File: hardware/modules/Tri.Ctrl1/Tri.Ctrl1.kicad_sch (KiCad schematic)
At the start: 1 part

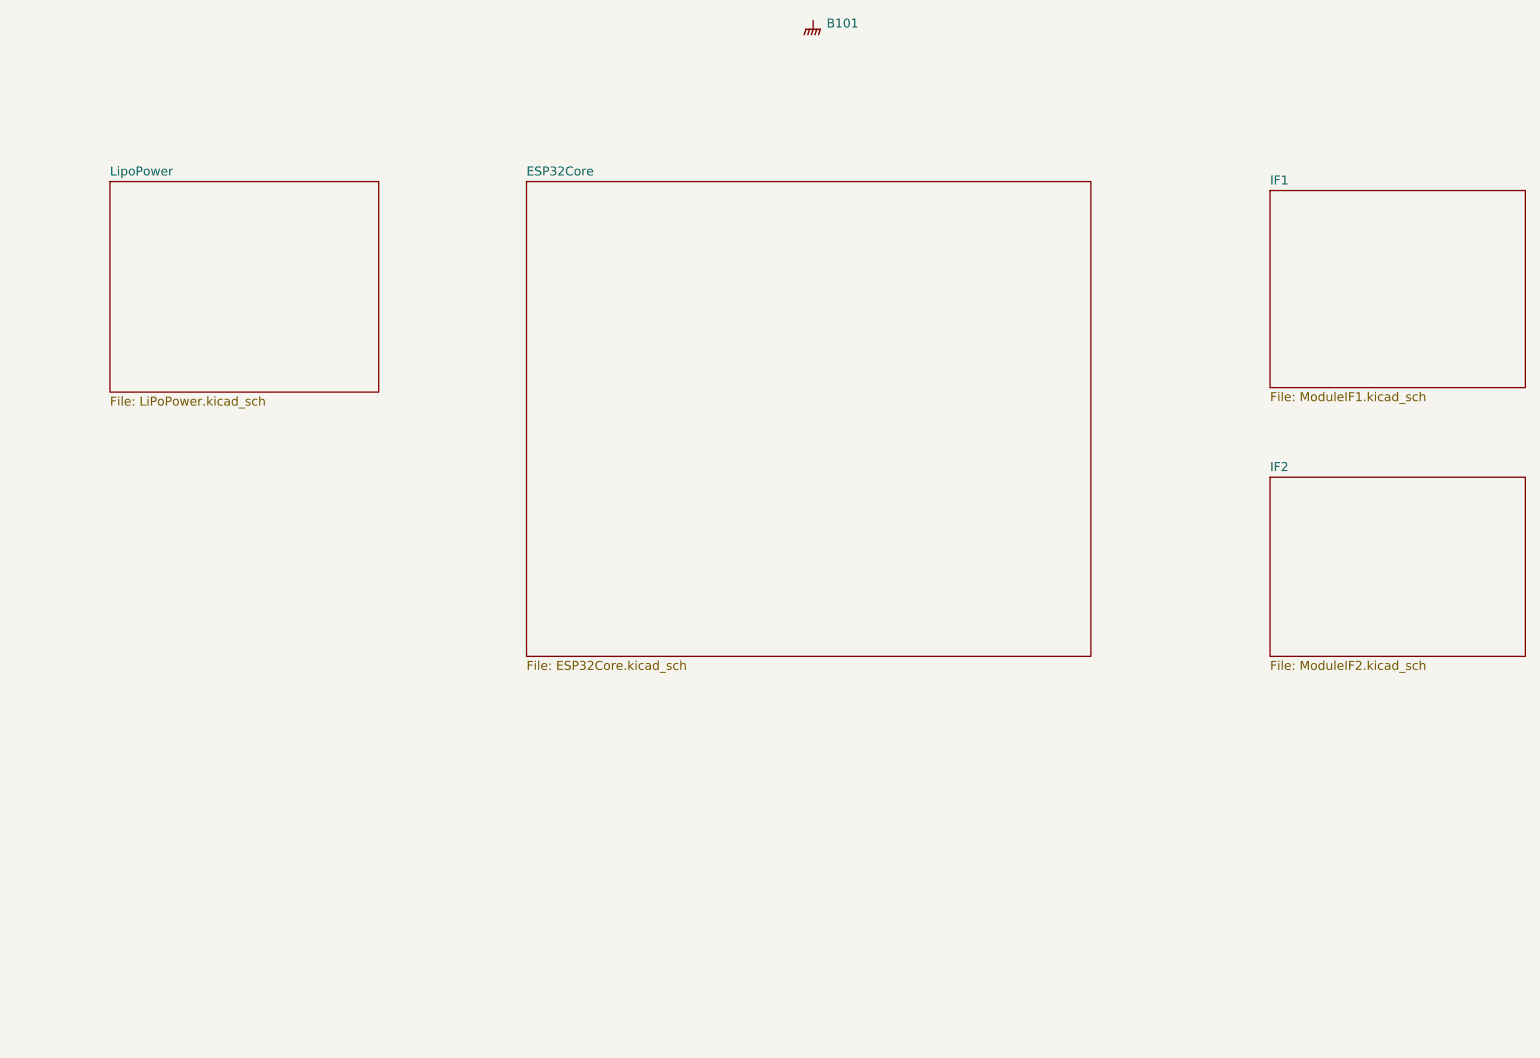
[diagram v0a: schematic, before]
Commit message: 回路図　半分終わり
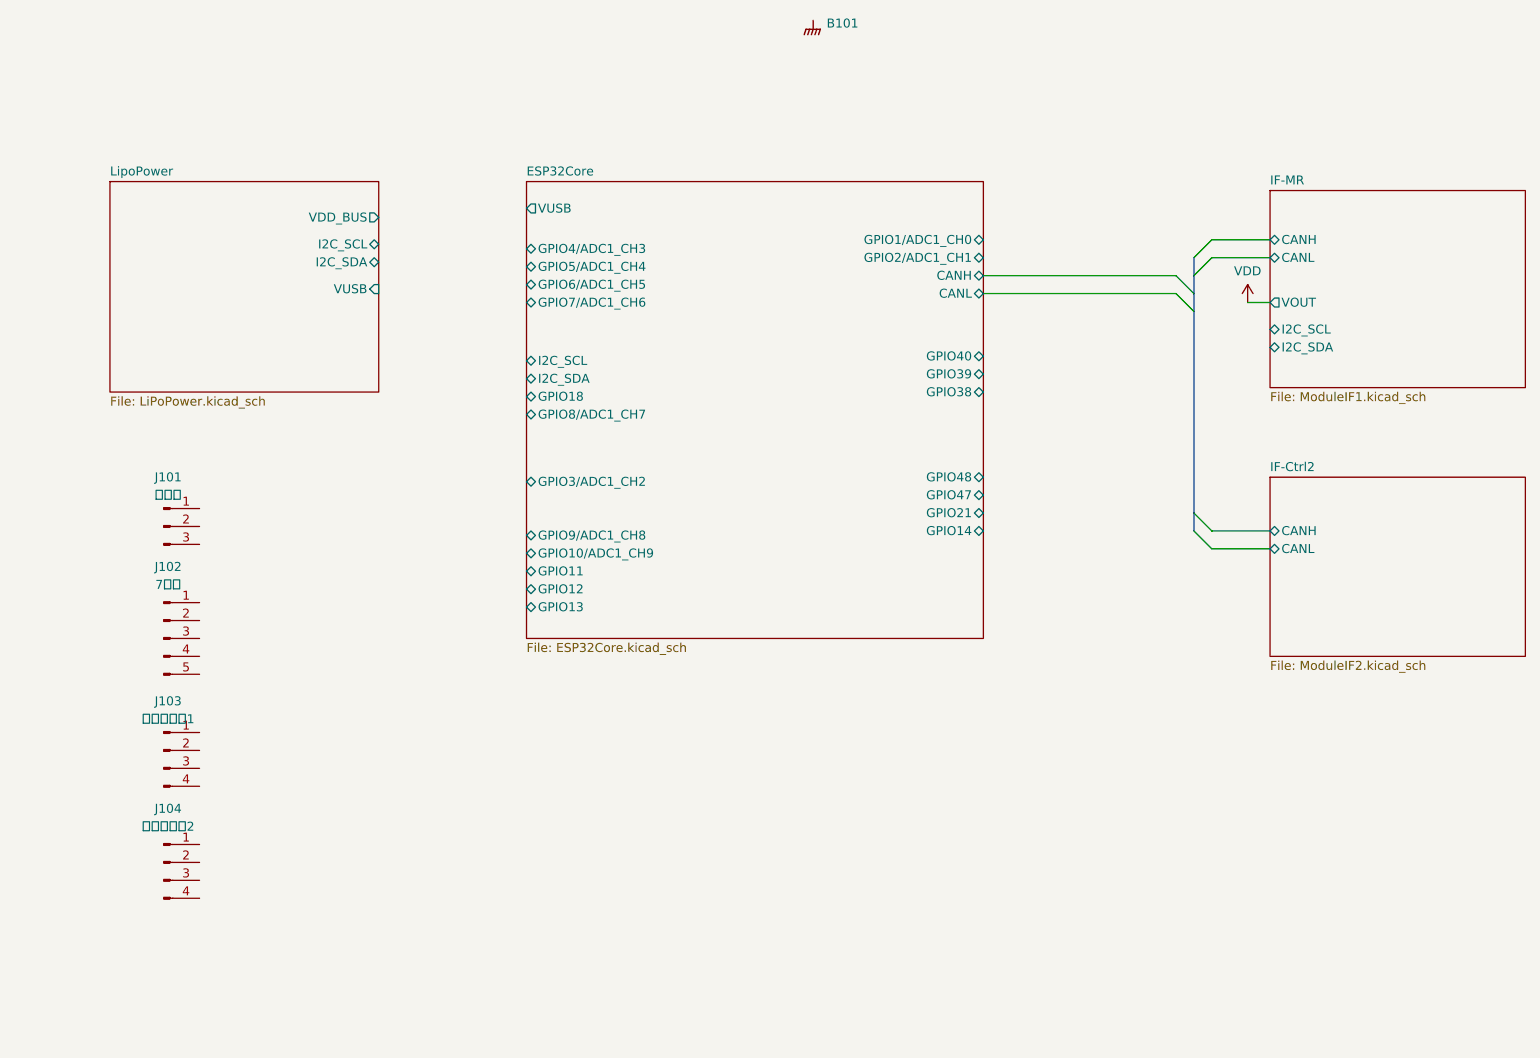
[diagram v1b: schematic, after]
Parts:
- added J101: トリム, symbol Connector:Conn_01x03_Pin
- added J102: 7セグ, symbol Connector:Conn_01x05_Pin
- added J103: ジョイコン1, symbol Connector:Conn_01x04_Pin
- added J104: ジョイコン2, symbol Connector:Conn_01x04_Pin
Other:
- sheet IF1 renamed IF-MR
- sheet IF2 renamed IF-Ctrl2
- sheet ESP32Core ports: added CANH, CANL, GPIO10/ADC1_CH9, GPIO11, GPIO12, GPIO13, GPIO14, GPIO18, GPIO1/ADC1_CH0, GPIO21, GPIO2/ADC1_CH1, GPIO38, GPIO39, GPIO3/ADC1_CH2, GPIO40, GPIO47, GPIO48, GPIO4/ADC1_CH3, GPIO5/ADC1_CH4, GPIO6/ADC1_CH5, GPIO7/ADC1_CH6, GPIO8/ADC1_CH7, GPIO9/ADC1_CH8, I2C_SCL, I2C_SDA, VUSB; removed none
- sheet IF-Ctrl2 ports: added CANH, CANL; removed none
- sheet IF-MR ports: added CANH, CANL, I2C_SCL, I2C_SDA, VOUT; removed none
- sheet LipoPower ports: added I2C_SCL, I2C_SDA, VDD_BUS, VUSB; removed none

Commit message: 回路図終了
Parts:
- B101: footprint (none) -> WOBCLibrary:Board_1U_60x60
- J101: renamed from J103; footprint (none) -> Connector_JST:JST_XA_S04B-XASK-1N-BN_1x04_P2.50mm_Horizontal
- J102: renamed from J104; footprint (none) -> Connector_JST:JST_XA_S04B-XASK-1N-BN_1x04_P2.50mm_Horizontal
- J103: renamed from J101; footprint (none) -> Connector_JST:JST_XA_B03B-XASK-1_1x03_P2.50mm_Vertical
- J104: renamed from J102; footprint (none) -> Connector_JST:JST_XA_B05B-XASK-1_1x05_P2.50mm_Vertical
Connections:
- net ESP32Core/GPIO10/ADC1_CH9: now also J101.3 (Pin_3)
- net ESP32Core/GPIO11: now also J102.2 (Pin_2)
- net ESP32Core/GPIO12: now also J102.3 (Pin_3)
- net ESP32Core/GPIO9/ADC1_CH8: now also J101.2 (Pin_2)
- net GND: now also J101.4 (Pin_4), J102.4 (Pin_4), J103.3 (Pin_3), J104.2 (Pin_2)
- net VDD: now also J101.1 (Pin_1), J102.1 (Pin_1), J104.1 (Pin_1)
- net UP: now reaches J103.1 (Pin_1)
- net DOWN: now reaches J103.2 (Pin_2)
- net SDI: now reaches J104.3 (Pin_3)
- net SCK: now reaches J104.4 (Pin_4)
- net LATCH: now reaches J104.5 (Pin_5)
- no-connect marks 0 -> 12
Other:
- moved on the sheet: J101, J102, J103, J104

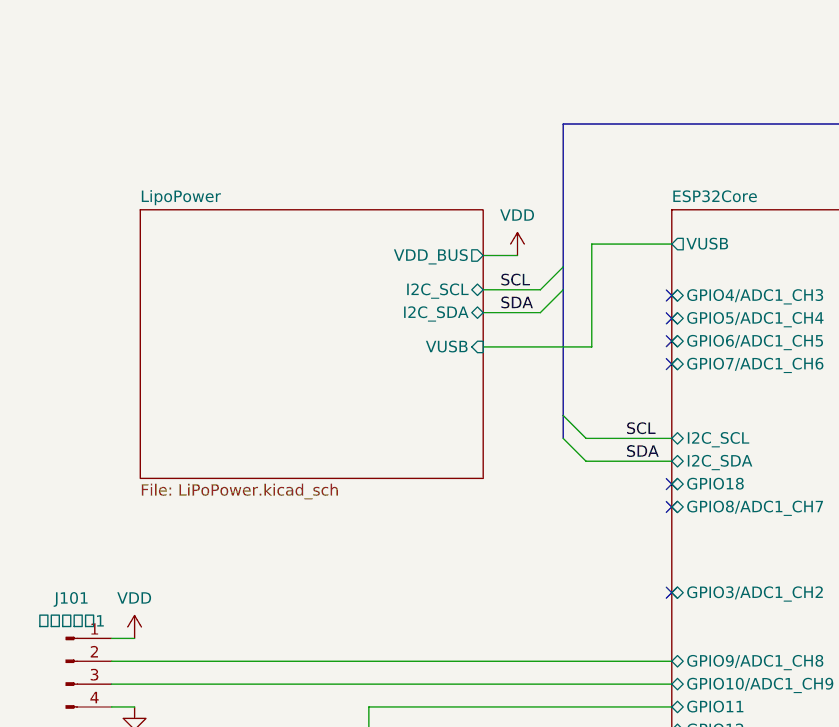
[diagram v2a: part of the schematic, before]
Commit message: 電源回路をlipoの充放電込みのモノに変更
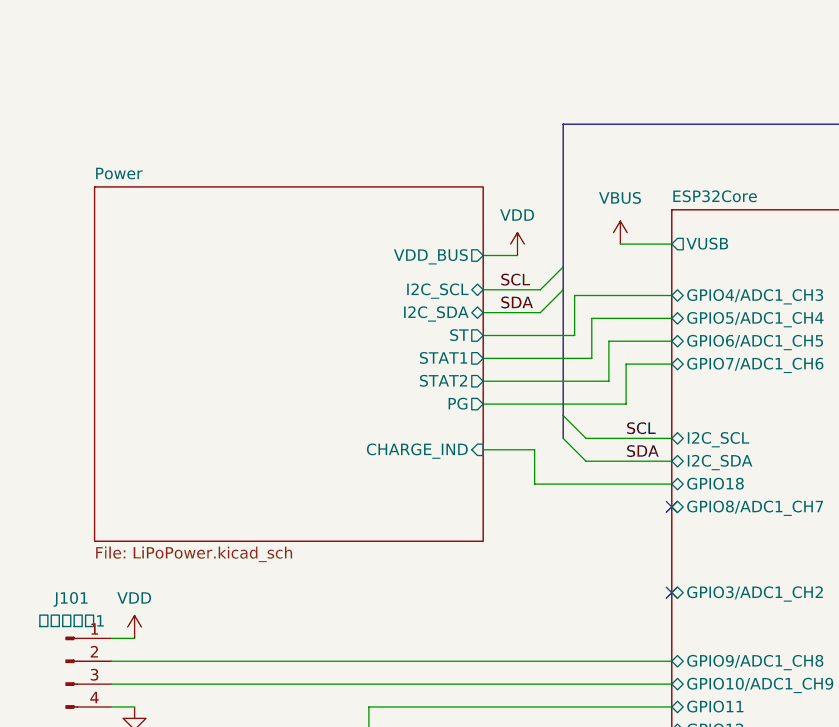
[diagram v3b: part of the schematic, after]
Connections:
- no-connect marks 12 -> 7
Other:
- removed sheet LipoPower
- added sheet Power (LiPoPower.kicad_sch)

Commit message: バックアップの回路削除
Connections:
- no-connect marks 7 -> 8
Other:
- sheet Power ports: added none; removed ST
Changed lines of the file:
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@@
 		(at 92.075 123.825)
+	)
+	(no_connect
+		(at 92.075 73.025)
 	)
 	(bus_entry
@@
 	(wire
 		(pts
-			(xy 92.075 73.025) (xy 81.28 73.025)
-		)
-		(stroke
-			(width 0)
-			(type default)
-		)
-	)
-	(wire
-		(pts
 			(xy 78.74 182.88) (xy 106.045 182.88)
 		)
@@
 	(wire
 		(pts
-			(xy 81.28 73.025) (xy 81.28 77.47)
-		)
-		(stroke
-			(width 0)
-			(type default)
-		)
-	)
-	(wire
-		(pts
 			(xy 156.845 76.835) (xy 184.15 76.835)
 		)
@@
 		(pts
 			(xy 71.12 80.01) (xy 83.185 80.01)
-		)
-		(stroke
-			(width 0)
-			(type default)
-		)
-	)
-	(wire
-		(pts
-			(xy 81.28 77.47) (xy 71.12 77.47)
 		)
 		(stroke
@@
 		(dnp no)
 		(fields_autoplaced yes)
-		(property "Reference" "#PWR0109"
+		(property "Reference" "#PWR0110"
 			(at 194.31 84.455 0)
 			(effects
@@
 			(project ""
 				(path "/39a3f286-a766-4612-a8bf-4e53d682d5ae"
-					(reference "#PWR0109")
+					(reference "#PWR0110")
 					(unit 1)
 				)
@@
 		(dnp no)
 		(fields_autoplaced yes)
-		(property "Reference" "#PWR0112"
+		(property "Reference" "#PWR0109"
 			(at 86.36 71.12 0)
 			(effects
@@
 			(project ""
 				(path "/39a3f286-a766-4612-a8bf-4e53d682d5ae"
-					(reference "#PWR0112")
+					(reference "#PWR0109")
 					(unit 1)
 				)
@@
 			(effects
 				(font
-					(size 1.27 1.27)
-				)
-				(justify right)
-			)
-		)
-		(pin "ST" output
-			(at 71.12 77.47 0)
-			(effects
-				(font

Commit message: 配置ちょっと進捗を
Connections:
- no-connect marks 8 -> 7
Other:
- sheet IF-MR ports: added EN, VIN; removed VOUT
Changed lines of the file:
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@@
-	)
-	(no_connect
-		(at 156.845 74.295)
 	)
 	(no_connect
@@
 	(wire
 		(pts
+			(xy 178.435 74.295) (xy 178.435 67.945)
+		)
+		(stroke
+			(width 0)
+			(type default)
+		)
+	)
+	(wire
+		(pts
 			(xy 189.23 113.03) (xy 197.485 113.03)
 		)
@@
 	(wire
 		(pts
+			(xy 178.435 67.945) (xy 197.485 67.945)
+		)
+		(stroke
+			(width 0)
+			(type default)
+		)
+	)
+	(wire
+		(pts
 			(xy 74.93 175.26) (xy 81.28 175.26)
 		)
@@
 		(pts
 			(xy 166.37 115.57) (xy 166.37 137.795)
+		)
+		(stroke
+			(width 0)
+			(type default)
+		)
+	)
+	(wire
+		(pts
+			(xy 156.845 74.295) (xy 178.435 74.295)
 		)
 		(stroke
@@
 			)
 		)
-		(pin "VOUT" output
-			(at 197.485 80.645 180)
-			(effects
-				(font
-					(size 1.27 1.27)
-				)
-				(justify left)
-			)
-		)
 		(pin "I2C_SCL" bidirectional
 			(at 197.485 84.455 180)
@@
 			(effects
 				(font
+					(size 1.27 1.27)
+				)
+				(justify left)
+			)
+		)
+		(pin "VIN" input
+			(at 197.485 80.645 180)
+			(effects
+				(font
+					(size 1.27 1.27)
+				)
+				(justify left)
+			)
+		)
+		(pin "EN" input
+			(at 197.485 67.945 180)
+			(effects
+				(font

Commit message: 配線2/3
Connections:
- net ESP32Core/GPIO10/ADC1_CH9 is gone; now on net ESP32Core/GPIO4/ADC1_CH3: J101.3 (Pin_3)
- net ESP32Core/GPIO11 is gone; now on net ESP32Core/GPIO9/ADC1_CH8: J102.2 (Pin_2)
- net ESP32Core/GPIO12 is gone; now on net ESP32Core/GPIO3/ADC1_CH2: J102.3 (Pin_3)
- net ESP32Core/GPIO5/ADC1_CH4: now also J101.2 (Pin_2)
- net ESP32Core/GPIO9/ADC1_CH8: no longer J101.2 (Pin_2)
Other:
- moved on the sheet: J103, J104

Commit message: とりあえず一通り配線
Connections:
- net ESP32Core/GPIO4/ADC1_CH3: now also J101.2 (Pin_2); no longer J101.3 (Pin_3)
- net ESP32Core/GPIO5/ADC1_CH4: now also J101.3 (Pin_3); no longer J101.2 (Pin_2)
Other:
- moved on the sheet: B101, J103
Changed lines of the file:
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@@
 	(paper "A4")
 	(no_connect
+		(at 156.845 74.295)
+	)
+	(no_connect
 		(at 92.075 96.52)
 	)
@@
 	)
 	(no_connect
-		(at 92.075 78.105)
-	)
-	(no_connect
 		(at 92.075 80.645)
 	)
@@
 	)
 	(bus_entry
-		(at 163.83 176.53)
+		(at 163.83 153.035)
 		(size 2.54 -2.54)
 		(stroke
@@
 	)
 	(bus_entry
-		(at 163.83 173.99)
+		(at 163.83 150.495)
 		(size 2.54 -2.54)
 		(stroke
@@
 	(bus
 		(pts
-			(xy 166.37 171.45) (xy 166.37 173.99)
+			(xy 166.37 147.955) (xy 166.37 150.495)
+		)
+		(stroke
+			(width 0)
+			(type default)
+		)
+	)
+	(wire
+		(pts
+			(xy 86.995 78.105) (xy 86.995 60.325)
 		)
 		(stroke
@@
 		)
 	)
+	(wire
+		(pts
+			(xy 85.725 75.565) (xy 85.725 102.87)
+		)
+		(stroke
+			(width 0)
+			(type default)
+		)
+	)
 	(bus
 		(pts
@@
 	(wire
 		(pts
-			(xy 148.59 176.53) (xy 163.83 176.53)
+			(xy 148.59 153.035) (xy 163.83 153.035)
 		)
 		(stroke
@@
 	(wire
 		(pts
-			(xy 85.725 102.87) (xy 85.725 73.025)
-		)
-		(stroke
-			(width 0)
-			(type default)
-		)
-	)
-	(wire
-		(pts
 			(xy 173.355 84.455) (xy 197.485 84.455)
 		)
@@
 	(wire
 		(pts
-			(xy 148.59 173.99) (xy 163.83 173.99)
+			(xy 148.59 150.495) (xy 163.83 150.495)
 		)
 		(stroke
@@
 	(wire
 		(pts
-			(xy 85.725 73.025) (xy 92.075 73.025)
+			(xy 84.455 73.025) (xy 92.075 73.025)
 		)
 		(stroke
@@
 	(wire
 		(pts
-			(xy 84.455 75.565) (xy 92.075 75.565)
-		)
-		(stroke
-			(width 0)
-			(type default)
-		)
-	)
-	(wire
-		(pts
 			(xy 189.23 74.295) (xy 197.485 74.295)
 		)
@@
 	(wire
 		(pts
-			(xy 178.435 74.295) (xy 178.435 67.945)
-		)
-		(stroke
-			(width 0)
-			(type default)
-		)
-	)
-	(wire
-		(pts
 			(xy 189.23 113.03) (xy 197.485 113.03)
 		)
@@
 	(wire
 		(pts
-			(xy 178.435 67.945) (xy 197.485 67.945)
-		)
-		(stroke
-			(width 0)
-			(type default)
-		)
-	)
-	(wire
-		(pts
 			(xy 47.625 156.845) (xy 53.975 156.845)
 		)
@@
 	(wire
 		(pts
-			(xy 84.455 75.565) (xy 84.455 101.6)
+			(xy 84.455 73.025) (xy 84.455 101.6)
 		)
 		(stroke
@@
 		)
 	)
+	(wire
+		(pts
+			(xy 92.075 78.105) (xy 86.995 78.105)
+		)
+		(stroke
+			(width 0)
+			(type default)
+		)
+	)
 	(bus
 		(pts
@@
 		)
 	)
+	(wire
+		(pts
+			(xy 86.995 60.325) (xy 164.465 60.325)
+		)
+		(stroke
+			(width 0)
+			(type default)
+		)
+	)
 	(bus
 		(pts
@@
 	(wire
 		(pts
+			(xy 92.075 75.565) (xy 85.725 75.565)
+		)
+		(stroke
+			(width 0)
+			(type default)
+		)
+	)
+	(wire
+		(pts
 			(xy 47.625 154.305) (xy 56.515 154.305)
 		)
@@
 	(wire
 		(pts
-			(xy 148.59 179.07) (xy 151.13 179.07)
+			(xy 148.59 155.575) (xy 151.13 155.575)
 		)
 		(stroke
@@
 	(wire
 		(pts
+			(xy 164.465 60.325) (xy 164.465 67.945)
+		)
+		(stroke
+			(width 0)
+			(type default)
+		)
+	)
+	(wire
+		(pts
 			(xy 83.82 118.745) (xy 92.075 118.745)
 		)
@@
 	(wire
 		(pts
-			(xy 92.075 67.31) (xy 88.265 67.31)
+			(xy 92.075 67.31) (xy 90.17 67.31)
 		)
 		(stroke
@@
 	(bus
 		(pts
-			(xy 166.37 115.57) (xy 166.37 171.45)
-		)
-		(stroke
-			(width 0)
-			(type default)
-		)
-	)
-	(wire
-		(pts
-			(xy 156.845 74.295) (xy 178.435 74.295)
+			(xy 166.37 115.57) (xy 166.37 147.955)
 		)
 		(stroke
@@
 		(pts
 			(xy 167.64 85.725) (xy 167.64 88.265)
+		)
+		(stroke
+			(width 0)
+			(type default)
+		)
+	)
+	(wire
+		(pts
+			(xy 164.465 67.945) (xy 197.485 67.945)
 		)
 		(stroke
@@
 	)
 	(label "UP"
-		(at 155.575 173.99 0)
+		(at 155.575 150.495 0)
 		(fields_autoplaced yes)
 		(effects
@@
 	)
 	(label "DOWN"
-		(at 155.575 176.53 0)
+		(at 155.575 153.035 0)
 		(fields_autoplaced yes)
 		(effects
@@
 	(symbol
 		(lib_id "Connector:Conn_01x03_Pin")
-		(at 143.51 176.53 0)
+		(at 143.51 153.035 0)
 		(unit 1)
 		(exclude_from_sim no)
@@
 		(fields_autoplaced yes)
 		(property "Reference" "J103"
-			(at 144.145 169.545 0)
+			(at 144.145 146.05 0)
 			(effects
 				(font
@@
 		)
 		(property "Value" "トリム"
-			(at 144.145 172.085 0)
+			(at 144.145 148.59 0)
 			(effects
 				(font
@@
 		)
 		(property "Footprint" "Connector_JST:JST_XA_B03B-XASK-1_1x03_P2.50mm_Vertical"
-			(at 143.51 176.53 0)
+			(at 143.51 153.035 0)
 			(effects
 				(font
@@
 		)
 		(property "Datasheet" "~"
-			(at 143.51 176.53 0)
+			(at 143.51 153.035 0)
 			(effects
 				(font
@@
 		)
 		(property "Description" "Generic connector, single row, 01x03, script generated"
-			(at 143.51 176.53 0)
+			(at 143.51 153.035 0)
 			(effects
 				(font
@@
 	(symbol
 		(lib_id "WOBCLibrary:Board")
-		(at 132.715 40.64 0)
+		(at 123.825 43.18 0)
 		(unit 1)
 		(exclude_from_sim no)
@@
 		(fields_autoplaced yes)
 		(property "Reference" "B101"
-			(at 134.62 41.0717 0)
+			(at 125.73 43.6117 0)
 			(effects
 				(font
@@
 		)
 		(property "Value" "~"
-			(at 134.62 42.9768 0)
+			(at 125.73 45.5168 0)
 			(effects
 				(font
@@
 		)
 		(property "Footprint" "WOBCLibrary:Board_1U_60x60"
-			(at 132.715 40.64 0)
+			(at 123.825 43.18 0)
 			(effects
 				(font
@@
 		)
 		(property "Datasheet" ""
-			(at 132.715 40.64 0)
+			(at 123.825 43.18 0)
 			(effects
 				(font
@@
 		)
 		(property "Description" ""
-			(at 132.715 40.64 0)
+			(at 123.825 43.18 0)
 			(effects
 				(font
@@
 	(symbol
 		(lib_id "power:GND")
-		(at 151.13 179.07 0)
+		(at 151.13 155.575 0)
 		(unit 1)
 		(exclude_from_sim no)
@@
 		(fields_autoplaced yes)
 		(property "Reference" "#PWR0106"
-			(at 151.13 185.42 0)
+			(at 151.13 161.925 0)
 			(effects
 				(font
@@
 		)
 		(property "Value" "GND"
-			(at 151.13 183.515 0)
+			(at 151.13 160.02 0)
 			(effects
 				(font
@@
 		)
 		(property "Footprint" ""
-			(at 151.13 179.07 0)
+			(at 151.13 155.575 0)
 			(effects
 				(font
@@
 		)
 		(property "Datasheet" ""
-			(at 151.13 179.07 0)
+			(at 151.13 155.575 0)
 			(effects
 				(font
@@
 		)
 		(property "Description" "Power symbol creates a global label with name \"GND\" , ground"
-			(at 151.13 179.07 0)
+			(at 151.13 155.575 0)
 			(effects
 				(font
@@
 	(symbol
 		(lib_id "power:VBUS")
-		(at 88.265 67.31 0)
+		(at 90.17 67.31 0)
 		(unit 1)
 		(exclude_from_sim no)
@@
 		(fields_autoplaced yes)
 		(property "Reference" "#PWR0109"
-			(at 88.265 71.12 0)
+			(at 90.17 71.12 0)
 			(effects
 				(font
@@
 		)
 		(property "Value" "VBUS"
-			(at 88.265 62.23 0)
+			(at 90.17 62.23 0)
 			(effects
 				(font
@@
 		)
 		(property "Footprint" ""
-			(at 88.265 67.31 0)
+			(at 90.17 67.31 0)
 			(effects
 				(font
@@
 		)
 		(property "Datasheet" ""
-			(at 88.265 67.31 0)
+			(at 90.17 67.31 0)
 			(effects
 				(font
@@
 		)
 		(property "Description" "Power symbol creates a global label with name \"VBUS\""
-			(at 88.265 67.31 0)
+			(at 90.17 67.31 0)
 			(effects
 				(font
@@
 		(at 92.075 63.5)
 		(size 64.77 64.77)
-		(fields_autoplaced yes)
 		(stroke
 			(width 0.1524)
@@
 		)
 		(property "Sheetname" "ESP32Core"
-			(at 92.075 62.7884 0)
-			(effects
-				(font
+			(at 93.726 62.738 0)
+			(effects
+				(font
